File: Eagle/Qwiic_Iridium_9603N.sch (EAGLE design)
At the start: 59 parts, among them J1 IRIDIUM_9603N, J3 PTH, J6 ISP, J7 U.FL, Q2 5.8A/30V/35mΩ, U1 ATTINY841SOIC, U2 LTC3225EDDB#TRMPBF, U3 ADM4210-1

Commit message: Generated PDF and cleaned up schematic
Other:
- note added: "10/28/2019"
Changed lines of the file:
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@@
 Current
 Limit</text>
+<text x="160.02" y="1.524" size="2.1844" layer="94">10/28/2019</text>
 </plain>
 <instances>
@@
 <instance part="FRAME1" gate="G$1" x="0" y="0" smashed="yes"/>
 <instance part="FRAME1" gate="V" x="147.32" y="0" smashed="yes">
-<attribute name="LAST_DATE_TIME" x="160.02" y="1.27" size="2.54" layer="94" font="vector"/>
 <attribute name="SHEET" x="233.68" y="1.27" size="2.54" layer="94" font="vector"/>
 <attribute name="DRAWING_NAME" x="162.814" y="17.78" size="2.7432" layer="94" font="vector"/>
@@
 <instance part="E1" gate="G$1" x="154.94" y="76.2" smashed="yes" rot="R270">
 <attribute name="NAME" x="149.86" y="70.612" size="1.778" layer="95" font="vector" rot="R270"/>
-<attribute name="VALUE" x="147.574" y="70.612" size="1.778" layer="96" font="vector" rot="R270"/>
 </instance>
 <instance part="U1" gate="U1" x="38.1" y="76.2" smashed="yes">
@@
 <instance part="Q2" gate="NMOS" x="228.6" y="175.26" smashed="yes" rot="R90">
 <attribute name="NAME" x="228.6" y="180.34" size="1.778" layer="95" font="vector" rot="R90"/>
-<attribute name="VALUE" x="231.14" y="180.34" size="1.778" layer="96" font="vector" rot="R90"/>
 </instance>
 </instances>

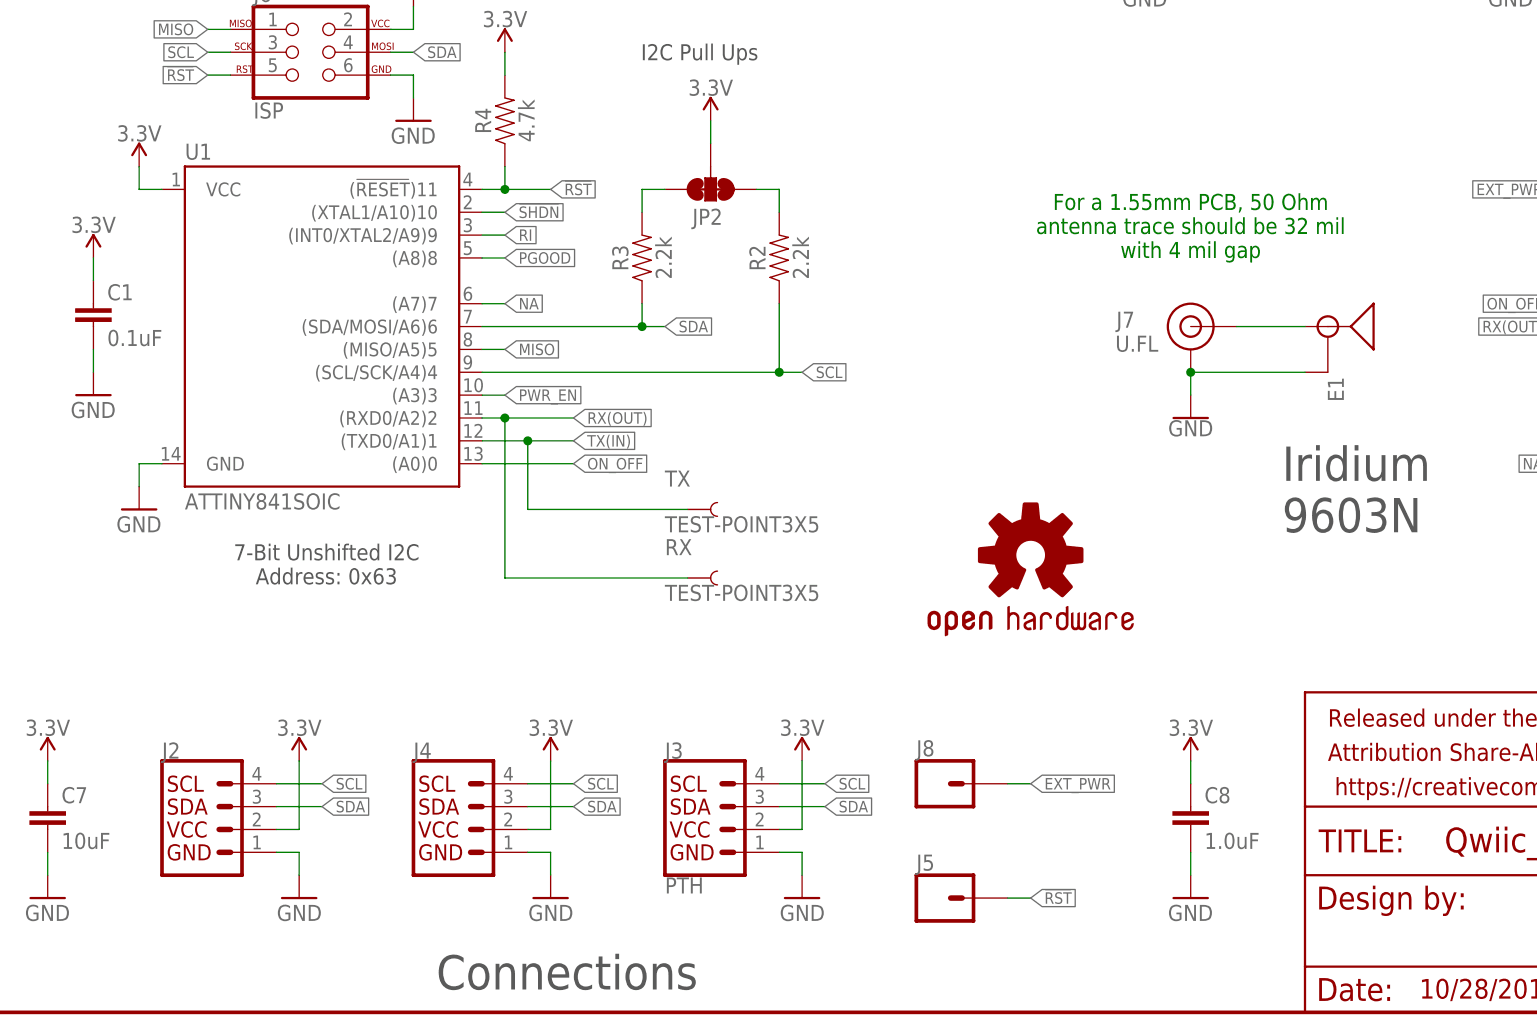
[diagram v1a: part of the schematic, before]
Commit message: Add ignore. Remove old backup files. Move TPs to bottom of board.
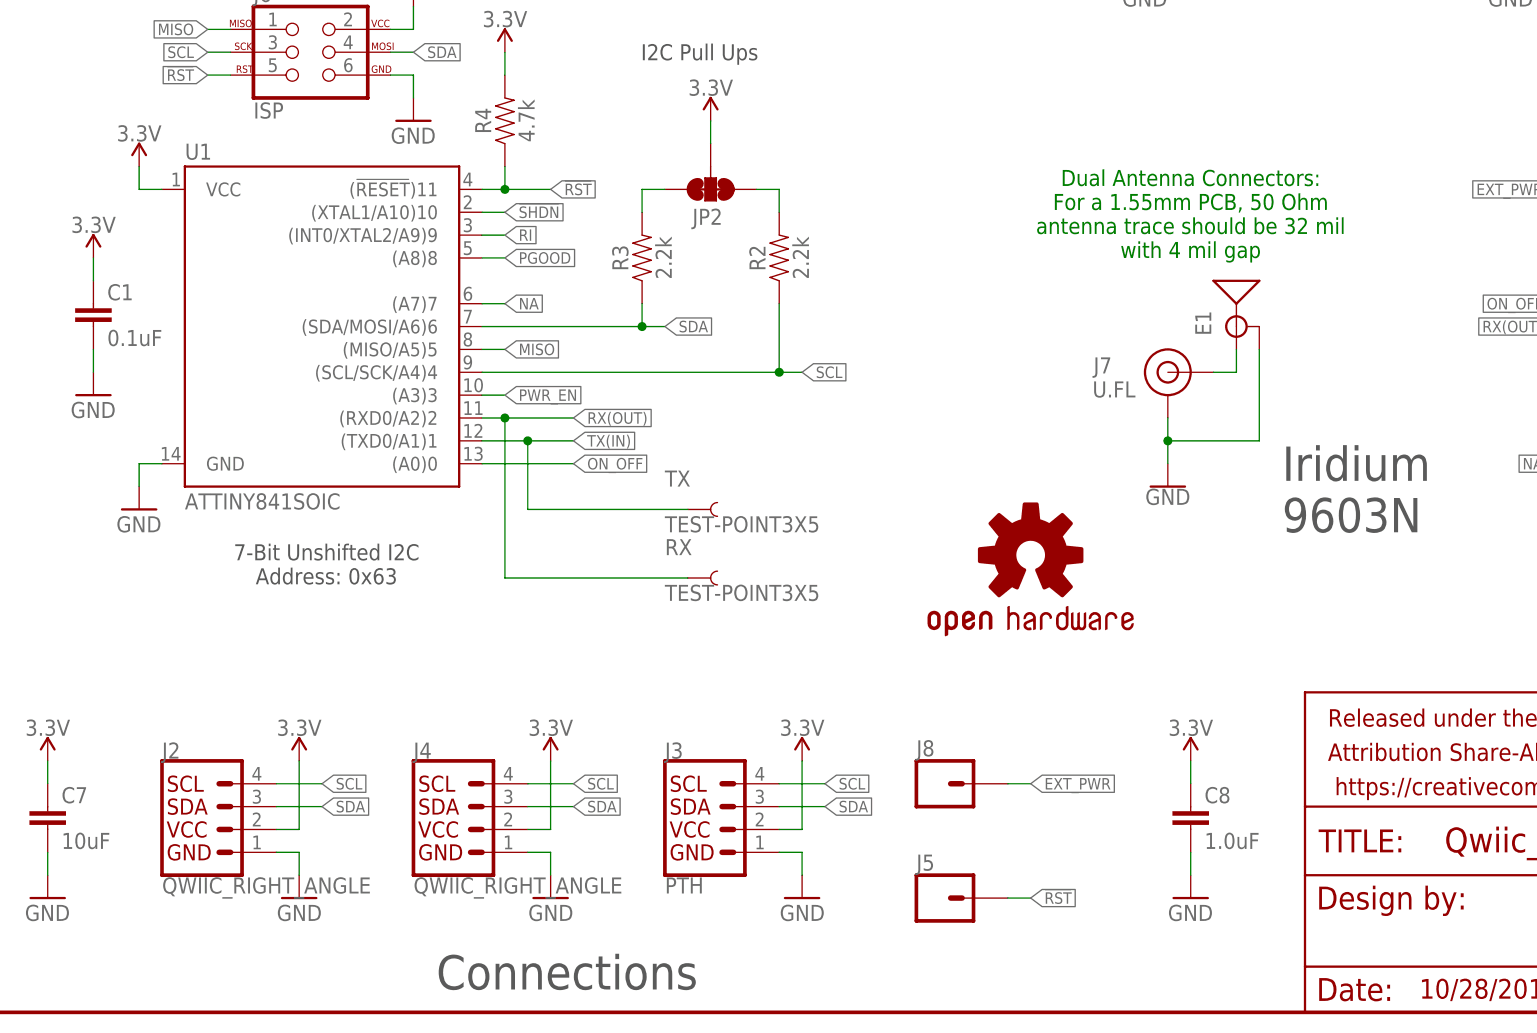
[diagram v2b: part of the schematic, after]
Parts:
- J2, J4: value (none) -> QWIIC_RIGHT_ANGLE
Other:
- note added: "Dual Antenna Connectors: For a 1.55mm PCB, 50 Ohm antenna trace should be 32 mil with 4 mil gap"
- note removed: "For a 1.55mm PCB, 50 Ohm antenna trace should be 32 mil with 4 mil gap"
- moved on the sheet: E1, J7
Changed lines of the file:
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@@
 <?xml version="1.0" encoding="utf-8"?>
 <!DOCTYPE eagle SYSTEM "eagle.dtd">
-<eagle version="9.4.2">
+<eagle version="9.5.2">
 <drawing>
 <settings>
@@
 <part name="JP6" library="SparkFun" deviceset="FIDUCIAL" device="UFIDUCIAL"/>
 <part name="SUPPLY4" library="SparkFun-PowerSymbols" deviceset="3.3V" device=""/>
-<part name="J2" library="SparkFun-Connectors" deviceset="QWIIC_CONNECTOR" device="JS-1MM"/>
+<part name="J2" library="SparkFun-Connectors" deviceset="QWIIC_CONNECTOR" device="JS-1MM" value="QWIIC_RIGHT_ANGLE"/>
 <part name="GND6" library="SparkFun-PowerSymbols" deviceset="GND" device=""/>
 <part name="SUPPLY7" library="SparkFun-PowerSymbols" deviceset="3.3V" device=""/>
@@
 <part name="FRAME1" library="SparkFun-Aesthetics" deviceset="FRAME-LETTER" device=""/>
 <part name="SUPPLY8" library="SparkFun-PowerSymbols" deviceset="3.3V" device=""/>
-<part name="J4" library="SparkFun-Connectors" deviceset="QWIIC_CONNECTOR" device="JS-1MM"/>
+<part name="J4" library="SparkFun-Connectors" deviceset="QWIIC_CONNECTOR" device="JS-1MM" value="QWIIC_RIGHT_ANGLE"/>
 <part name="GND8" library="SparkFun-PowerSymbols" deviceset="GND" device=""/>
 <part name="LOGO1" library="SparkFun-Aesthetics" deviceset="OSHW-LOGO" device="MINI"/>
@@
 <part name="R14" library="SparkFun-Resistors" library_urn="urn:adsk.eagle:library:532" deviceset="10KOHM" device="-0603-1/10W-1%" package3d_urn="urn:adsk.eagle:package:39650/1" value="10k"/>
 <part name="GND21" library="SparkFun-PowerSymbols" deviceset="GND" device=""/>
-<part name="PWR" library="SparkFun-Jumpers" deviceset="JUMPER-SMT_2_NC_TRACE" device="_SILK"/>
-<part name="JP1" library="SparkFun-Jumpers" deviceset="JUMPER-SMT_3_1-NC_TRACE" device="_SILK"/>
+<part name="PWR" library="SparkFun-Jumpers" deviceset="JUMPER-SMT_2_NC_TRACE" device="_SILK" package3d_urn="urn:adsk.eagle:package:39281/1"/>
+<part name="JP1" library="SparkFun-Jumpers" deviceset="JUMPER-SMT_3_1-NC_TRACE" device="_SILK" package3d_urn="urn:adsk.eagle:package:39288/1"/>
 <part name="E1" library="SparkFun-RF" deviceset="ANTENNA-GROUNDED" device="EDGE_SMA"/>
 <part name="U1" library="Qwiic_Iridium_9603N" deviceset="ATTINY841" device="SOIC"/>
@@
 <text x="144.78" y="53.34" size="3.81" layer="97" ratio="15">Iridium
 9603N</text>
-<text x="134.62" y="83.82" size="1.778" layer="91" align="bottom-center">For a 1.55mm PCB, 50 Ohm
+<text x="134.62" y="83.82" size="1.778" layer="91" align="bottom-center">Dual Antenna Connectors:
+For a 1.55mm PCB, 50 Ohm
 antenna trace should be 32 mil
 with 4 mil gap </text>
@@
 <attribute name="VALUE" x="122.442" y="168.89" size="1.27" layer="96" font="vector" rot="R90" align="center"/>
 </instance>
-<instance part="GND27" gate="1" x="134.62" y="66.04" smashed="yes">
-<attribute name="VALUE" x="134.62" y="65.786" size="1.778" layer="96" align="top-center"/>
-</instance>
-<instance part="J7" gate="G$1" x="134.62" y="76.2" smashed="yes">
-<attribute name="NAME" x="126.365" y="76.073" size="1.778" layer="95"/>
-<attribute name="VALUE" x="126.238" y="73.406" size="1.778" layer="96"/>
+<instance part="GND27" gate="1" x="132.08" y="58.42" smashed="yes">
+<attribute name="VALUE" x="132.08" y="58.166" size="1.778" layer="96" align="top-center"/>
+</instance>
+<instance part="J7" gate="G$1" x="132.08" y="71.12" smashed="yes">
+<attribute name="NAME" x="123.825" y="70.993" size="1.778" layer="95"/>
+<attribute name="VALUE" x="123.698" y="68.326" size="1.778" layer="96"/>
 </instance>
 <instance part="SUPPLY5" gate="G$1" x="7.62" y="27.94" smashed="yes">
@@
 <attribute name="NAME" x="150.241" y="116.84" size="1.778" layer="95" font="vector" rot="R270"/>
 </instance>
-<instance part="E1" gate="G$1" x="154.94" y="76.2" smashed="yes" rot="R270">
-<attribute name="NAME" x="149.86" y="70.612" size="1.778" layer="95" font="vector" rot="R270"/>
+<instance part="E1" gate="G$1" x="139.7" y="76.2" smashed="yes">
+<attribute name="NAME" x="136.906" y="75.184" size="1.778" layer="95" font="vector" rot="R90"/>
 </instance>
 <instance part="U1" gate="U1" x="38.1" y="76.2" smashed="yes">
@@
 <pinref part="J7" gate="G$1" pin="GND"/>
 <pinref part="GND27" gate="1" pin="GND"/>
-<wire x1="134.62" y1="68.58" x2="134.62" y2="71.12" width="0.1524" layer="91"/>
-<wire x1="147.32" y1="71.12" x2="134.62" y2="71.12" width="0.1524" layer="91"/>
-<junction x="134.62" y="71.12"/>
+<wire x1="132.08" y1="60.96" x2="132.08" y2="63.5" width="0.1524" layer="91"/>
 <pinref part="E1" gate="G$1" pin="GND"/>
+<wire x1="132.08" y1="63.5" x2="132.08" y2="66.04" width="0.1524" layer="91"/>
+<wire x1="132.08" y1="63.5" x2="142.24" y2="63.5" width="0.1524" layer="91"/>
+<junction x="132.08" y="63.5"/>
+<wire x1="142.24" y1="63.5" x2="142.24" y2="73.66" width="0.1524" layer="91"/>
 </segment>
 <segment>
@@
 <segment>
 <pinref part="J7" gate="G$1" pin="SIGNAL"/>
-<wire x1="139.7" y1="76.2" x2="147.32" y2="76.2" width="0.1524" layer="91"/>
 <pinref part="E1" gate="G$1" pin="SIGNAL"/>
-</segment>
-</net>
+<wire x1="139.7" y1="73.66" x2="139.7" y2="71.12" width="0.1524" layer="91"/>
+<wire x1="139.7" y1="71.12" x2="137.16" y2="71.12" width="0.1524" layer="91"/>
+</segment>
+</net>

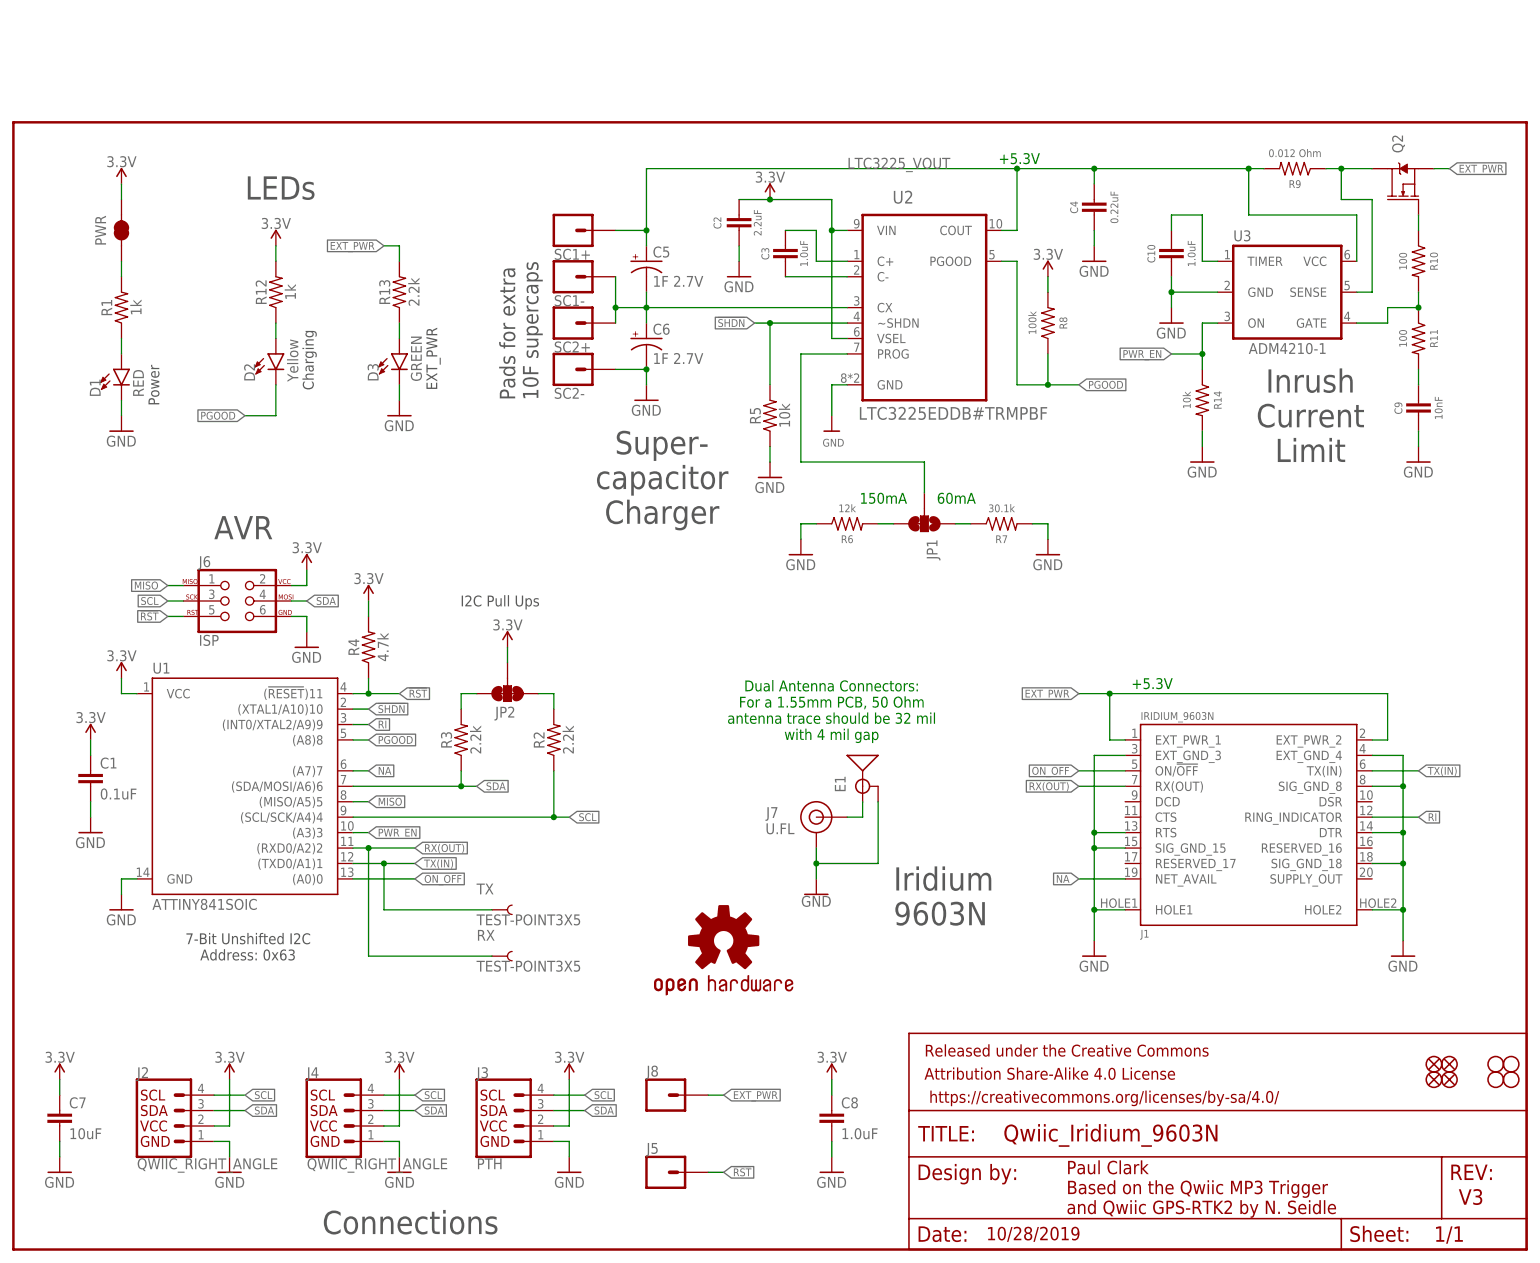
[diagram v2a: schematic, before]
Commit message: Update connector footprint: reduce cream, extend copper, remove extra silk.
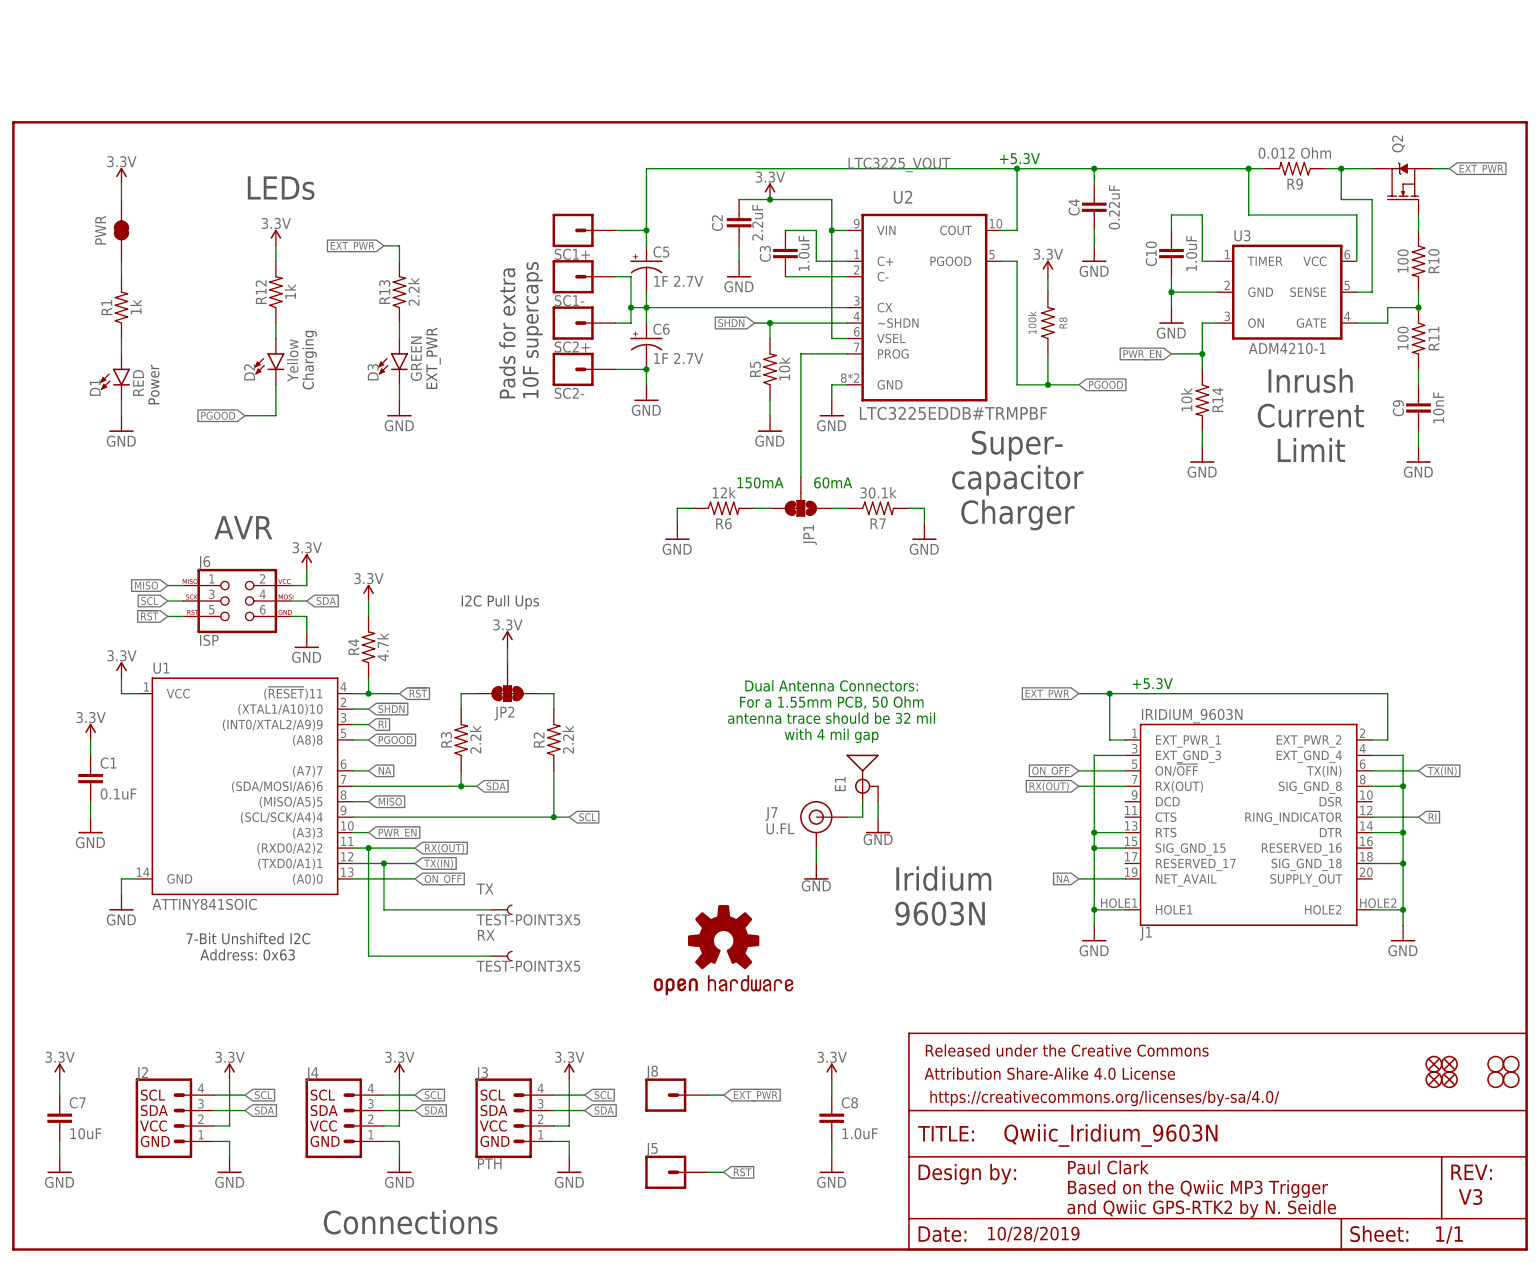
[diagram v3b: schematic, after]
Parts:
- J2, J4: value QWIIC_RIGHT_ANGLE -> (none)
- JP10, JP3, JP4, JP9: device SparkFun:STAND-OFF -> SparkFun-Hardware:STAND-OFF
- JP5, JP6, JP7, JP8: value FIDUCIALUFIDUCIAL -> FIDUCIAL1X2; device SparkFun:FIDUCIALUFIDUCIAL -> SparkFun-Aesthetics:FIDUCIAL1X2
- R1, R12: device SparkFun-Resistors:1KOHM-0603-1/10W-1% -> Qwiic_Iridium_9603N:1KOHM-0603-1/10W-1%
- U3: device ADM4210:ADM4210-1 -> Qwiic_Iridium_9603N:ADM4210-1
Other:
- moved on the sheet: JP1, R5, R6, R7
